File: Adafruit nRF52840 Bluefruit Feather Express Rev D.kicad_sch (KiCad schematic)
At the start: 41 parts, among them IC2 GD25Q16, J1 USB_C_Receptacle_USB2.0, Q3 DMG2305, SW101 KMR2, SW102 KMR2, U0 USBLC6-2SC6, U2 AP2112(3.3V), U3 MCP73831T-2ACI/OT, X3 JSTPH, Y2 32.768

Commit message: Small work
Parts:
- removed D+0, D-0: TPTP10R, Adafruit nRF52840 Bluefruit Feather Express Rev D:TP10R, symbol Adafruit nRF52840 Bluefruit Feather Express Rev D-eagle-import:TPTP10R
- removed J1: USB_C_Receptacle_USB2.0, JohnDeereLibrary:GCT USB4510-03-1-A, symbol Connector:USB_C_Receptacle_USB2.0
- removed R1, R6: 5.1k, Resistor_SMD:R_0603_1608Metric, symbol Device:R
- removed U0: USBLC6-2SC6, Package_TO_SOT_SMD:SOT-23-6, symbol Power_Protection:USBLC6-2SC6
- added J1: 781710004, CON_781710004, symbol 2023-09-18_17-26-43:781710004
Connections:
- net GND: now also J1.4, J1.5, J1.6
- net USBD+: now also J1.3
- net USBD-: now also J1.2
- net VBUS: now also J1.1

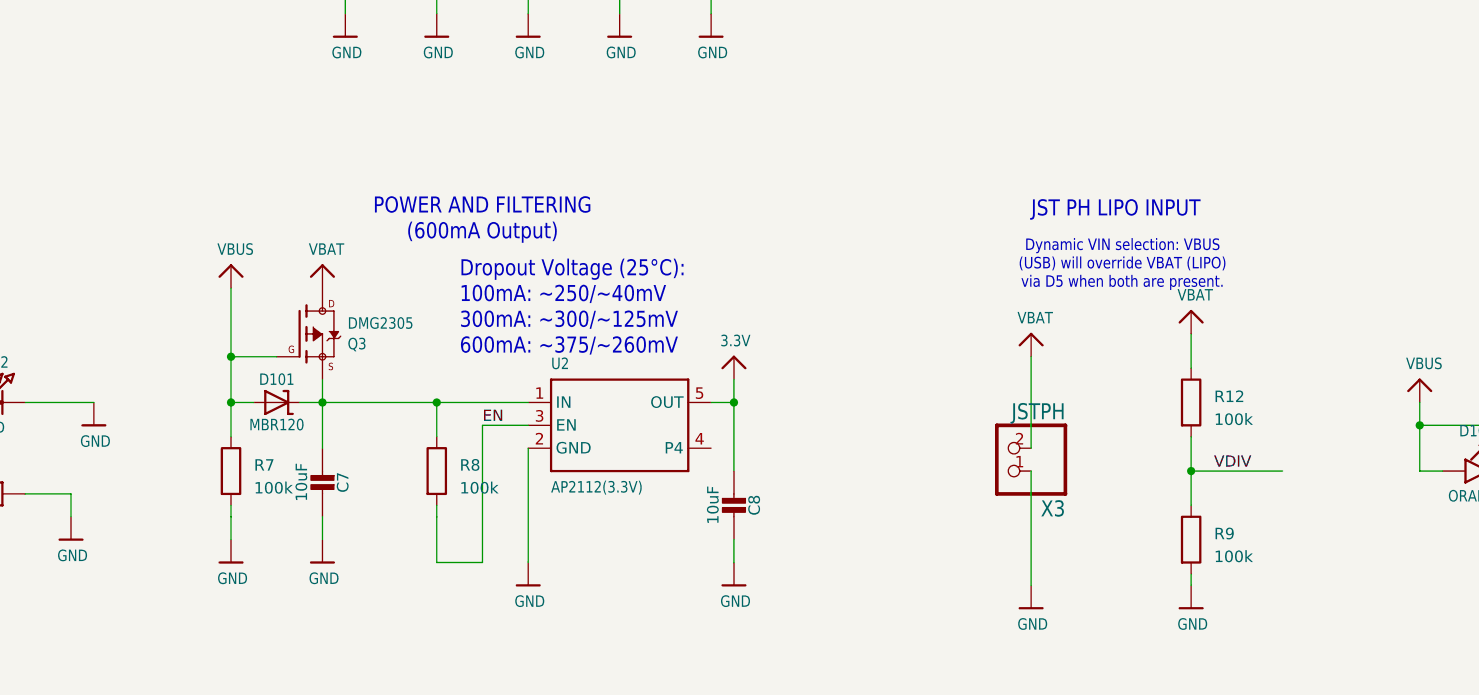
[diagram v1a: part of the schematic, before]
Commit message: removed bad diodes
TODO: rotate good diodes
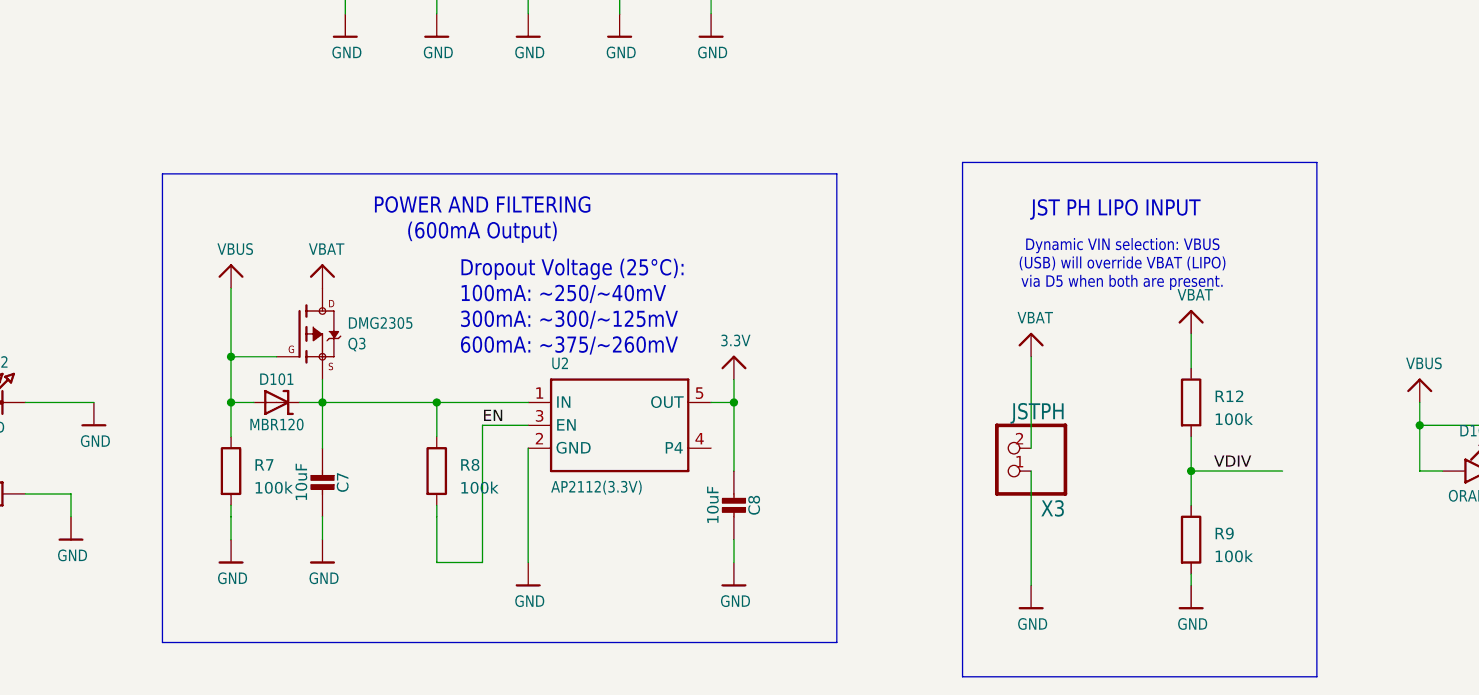
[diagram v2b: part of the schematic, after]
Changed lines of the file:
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@@
     (stroke (width 0.1524) (type solid))
+  )
+  (rectangle (start 170.18 212.09) (end 209.55 269.24)
+    (stroke (width 0.1) (type default) (color 128 77 0 1))
+    (fill (type none))
+  )
+  (rectangle (start 81.28 213.36) (end 156.21 265.43)
+    (stroke (width 0.1) (type default) (color 128 77 0 1))
+    (fill (type none))
   )
   (text "Dynamic VIN selection: VBUS\n(USB) will override VBAT (LIPO)\nvia D5 when both are present."
